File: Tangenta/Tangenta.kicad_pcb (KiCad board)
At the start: 4 copper layers, 243.8 x 243.8 mm, 183 parts, among them J1 39281243, J10 1-2199230-5, J11 TYPEC-304-ACP16, J12 907-211A1019D10200, J13 906-151A1058D10200, J14 RC01133, J16 TF-115K, J17 2309410-1, J18 1-2199230-5, J19 HYC90-SIM06-180, J2 Conn_02x02_Top_Bottom, J3 10018784-10213TLF, J4 10018784-10213TLF, J5 HY911130A, J6 HY911130A, J7 HY911130A, J8 HDMI_19PIN_043, J9 HC-SFP-01L, Q1 2N7002, Q2 2N7002, U1 TPS54331DR, U10 TUSB321RWBR, U11 AOZ1353DI-01, U12 PUSB2X4Y-N, U13 LT8912B, U2 TPS54331DR, U3 TPS54331DR, U4 TPS54331DR, U5 74HC74D,653, U6 CD4060SA_TR, U7 74HC04D,653, U8 USB2514B-I_M2, U9 PUSB2X4Y-N, X1 X322524MOB4SI

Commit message: Lontium - current progress...
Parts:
- added C80: 2.2nF, Capacitor_SMD:C_0402_1005Metric, F.Cu at (358.2, 66.4)
- added OSC1: OT322525MJBA4SL, 25MHZ_OSCILLATOR:25MHZ_OSCILLATOR, F.Cu at (349.7, 78.4)
- added R40: 100k, Resistor_SMD:R_0402_1005Metric, F.Cu at (360.7, 62.4)
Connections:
- U13 pad 1: unconnected-(U13A-MIPIRX0_DP-Pad1) -> /DSI_HDMI/DSI.D0_P
- U13 pad 10: unconnected-(U13A-MIPIRX2_DN-Pad10) -> /DSI_HDMI/DSI.D2_N
- U13 pad 11: unconnected-(U13A-MIPIRX3_DP-Pad11) -> /DSI_HDMI/DSI.D3_P
- U13 pad 12: unconnected-(U13A-MIPIRX3_DN-Pad12) -> /DSI_HDMI/DSI.D3_N
- U13 pad 14: (no net) -> /DSI_HDMI/DSI.HPD
- U13 pad 18: unconnected-(U13B-VDD-Pad18) -> /DSI_HDMI/VDD
- U13 pad 2: unconnected-(U13A-MIPIRX0_DN-Pad2) -> /DSI_HDMI/DSI.D0_N
- U13 pad 26: unconnected-(U13B-VCCA_HDMITX-Pad26) -> /DSI_HDMI/VCCA_HDMITX
- U13 pad 3: unconnected-(U13A-MIPIRX1_DP-Pad3) -> /DSI_HDMI/DSI.D1_P
- U13 pad 33: unconnected-(U13B-VDD-Pad33) -> /DSI_HDMI/VDD
- U13 pad 34: unconnected-(U13B-VCCA_HDMIPLL-Pad34) -> /DSI_HDMI/VCCA_HDMIPLL
- U13 pad 35: unconnected-(U13C-LPF-Pad35) -> Net-(U13C-LPF)
- U13 pad 4: unconnected-(U13A-MIPIRX1_DN-Pad4) -> /DSI_HDMI/DSI.D1_N
- U13 pad 41: unconnected-(U13B-VCCA_LVDSTX-Pad41) -> /DSI_HDMI/VCCA_LVDSTX
- U13 pad 5: unconnected-(U13B-VCCA_MIPIRX-Pad5) -> /DSI_HDMI/VCCA_MIPIRX
- U13 pad 50: unconnected-(U13B-VCCA_SYSCLK-Pad50) -> /DSI_HDMI/VCCA_SYSCLK
- U13 pad 52: unconnected-(U13B-VCCA_LVDSPLL-Pad52) -> /DSI_HDMI/VCCA_LVDSPLL
- U13 pad 57: unconnected-(U13B-VDD-Pad57) -> /DSI_HDMI/VDD
- U13 pad 63: unconnected-(U13C-INT-Pad63) -> /DSI_HDMI/DSI.INT
- U13 pad 64: unconnected-(U13C-RESET_N-Pad64) -> /DSI_HDMI/DSI.nRST
- U13 pad 7: unconnected-(U13A-MIPIRX_CKP-Pad7) -> /DSI_HDMI/DSI.CLK_P
- U13 pad 8: unconnected-(U13A-MIPIRX_CKN-Pad8) -> /DSI_HDMI/DSI.CLK_N
- U13 pad 9: unconnected-(U13A-MIPIRX2_DP-Pad9) -> /DSI_HDMI/DSI.D2_P

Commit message: DSI_HDMI current progress...
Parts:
- added C81: 10uF, Capacitor_SMD:C_0402_1005Metric, F.Cu at (338.1, 92.8)
- added C82: 100nF, Capacitor_SMD:C_0402_1005Metric, F.Cu at (338.1, 94.8)
- added C83: 10nF, Capacitor_SMD:C_0402_1005Metric, F.Cu at (338.1, 96.8)
- added FB9: GZ2012D101TF, Ferrite_Bead_100:Ferrite_Bead_100, F.Cu at (342.1, 93.5)
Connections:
- J17 pad 17: unconnected-(J17-Pad17) -> /DSI_HDMI/DSI.INT
- J17 pad 19: unconnected-(J17-Pad19) -> /DSI_HDMI/DSI.HPD
- J17 pad 21: unconnected-(J17-Pad21) -> /DSI_HDMI/DSI.nRST
- J17 pad 23: unconnected-(J17-Pad23) -> /DSI_HDMI/DSI.D3_N
- J17 pad 25: unconnected-(J17-Pad25) -> /DSI_HDMI/DSI.D3_P
- J17 pad 29: unconnected-(J17-Pad29) -> /DSI_HDMI/DSI.D2_N
- J17 pad 31: unconnected-(J17-Pad31) -> /DSI_HDMI/DSI.D2_P
- J17 pad 35: unconnected-(J17-Pad35) -> /DSI_HDMI/DSI.CLK_N
- J17 pad 37: unconnected-(J17-Pad37) -> /DSI_HDMI/DSI.CLK_P
- J17 pad 41: unconnected-(J17-Pad41) -> /DSI_HDMI/DSI.D1_N
- J17 pad 42: unconnected-(J17-Pad42) -> /DSI_HDMI/I2S.BCLK
- J17 pad 43: unconnected-(J17-Pad43) -> /DSI_HDMI/DSI.D1_P
- J17 pad 44: unconnected-(J17-Pad44) -> /DSI_HDMI/I2S.SYNC
- J17 pad 46: unconnected-(J17-Pad46) -> /DSI_HDMI/I2S.D_OUT
- J17 pad 47: unconnected-(J17-Pad47) -> /DSI_HDMI/DSI.D0_N
- J17 pad 49: unconnected-(J17-Pad49) -> /DSI_HDMI/DSI.D0_P
- OSC1 pad 1: unconnected-(OSC1-Enable/Disable-Pad1) -> Net-(OSC1-Enable/Disable)
- OSC1 pad 2: unconnected-(OSC1-GND-Pad2) -> GNDREF
- OSC1 pad 3: unconnected-(OSC1-OUT-Pad3) -> /DSI_HDMI/XTALI
- OSC1 pad 4: unconnected-(OSC1-VDD-Pad4) -> Net-(OSC1-Enable/Disable)
- U13 pad 53: unconnected-(U13A-XTALI-Pad53) -> /DSI_HDMI/XTALI
- U13 pad 58: unconnected-(U13C-SD0_CEC-Pad58) -> /DSI_HDMI/I2S.D_OUT
- U13 pad 59: unconnected-(U13C-WS_I-Pad59) -> /DSI_HDMI/I2S.SYNC
- U13 pad 60: unconnected-(U13C-SCLK_I-Pad60) -> /DSI_HDMI/I2S.BCLK

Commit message: Current progress...
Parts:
- added R41: 1.8k, Resistor_SMD:R_0402_1005Metric, F.Cu at (373.0, 63.9)
- added R42: 1.8k, Resistor_SMD:R_0402_1005Metric, F.Cu at (373.0, 65.9)
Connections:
- J17 pad 12: unconnected-(J17-Pad12) -> /Toradex/I2C.SDA
- J17 pad 14: unconnected-(J17-Pad14) -> /Toradex/I2C.SCL
- U13 pad 61: unconnected-(U13C-S_SDA-Pad61) -> /DSI_HDMI/I2C.SDA
- U13 pad 62: unconnected-(U13C-S_SCL-Pad62) -> /DSI_HDMI/I2C.SCL
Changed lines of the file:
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@@
   (net 648 "unconnected-(J17-Pad10)")
   (net 649 "unconnected-(J17-Pad11)")
-  (net 650 "unconnected-(J17-Pad12)")
+  (net 650 "/Toradex/I2C.SDA")
   (net 651 "unconnected-(J17-Pad13)")
-  (net 652 "unconnected-(J17-Pad14)")
+  (net 652 "/Toradex/I2C.SCL")
   (net 653 "unconnected-(J17-Pad15)")
   (net 654 "unconnected-(J17-Pad16)")
@@
   (net 1033 "unconnected-(U13C-XTALO-Pad54)")
   (net 1034 "unconnected-(U13C-REFCLK-Pad55)")
-  (net 1035 "unconnected-(U13C-S_SDA-Pad61)")
-  (net 1036 "unconnected-(U13C-S_SCL-Pad62)")
+  (net 1035 "/DSI_HDMI/I2C.SDA")
+  (net 1036 "/DSI_HDMI/I2C.SCL")
   (net 1037 "/DSI_HDMI/DSI.D3_N")
   (net 1038 "/DSI_HDMI/DSI.HPD")
@@
       (net 649 "unconnected-(J17-Pad11)") (pinfunction "11") (pintype "passive"))
     (pad "12" smd rect (at -30.625 -12.025 180) (size 0.3 1.75) (layers "F.Cu" "F.Paste" "F.Mask")
-      (net 650 "unconnected-(J17-Pad12)") (pinfunction "12") (pintype "passive"))
+      (net 650 "/Toradex/I2C.SDA") (pinfunction "12") (pintype "passive"))
     (pad "13" smd rect (at -30.375 -3.825 180) (size 0.3 1.75) (layers "F.Cu" "F.Paste" "F.Mask")
       (net 651 "unconnected-(J17-Pad13)") (pinfunction "13") (pintype "passive"))
     (pad "14" smd rect (at -30.125 -12.025 180) (size 0.3 1.75) (layers "F.Cu" "F.Paste" "F.Mask")
-      (net 652 "unconnected-(J17-Pad14)") (pinfunction "14") (pintype "passive"))
+      (net 652 "/Toradex/I2C.SCL") (pinfunction "14") (pintype "passive"))
     (pad "15" smd rect (at -29.875 -3.825 180) (size 0.3 1.75) (layers "F.Cu" "F.Paste" "F.Mask")
       (net 653 "unconnected-(J17-Pad15)") (pinfunction "15") (pintype "passive"))
@@
       (net 655 "/DSI_HDMI/I2S.BCLK") (pinfunction "SCLK_I") (pintype "unspecified") (thermal_bridge_angle 45))
     (pad "61" smd oval (at -1.8 -3.7) (size 0.2 0.7) (layers "F.Cu" "F.Paste" "F.Mask")
-      (net 1035 "unconnected-(U13C-S_SDA-Pad61)") (pinfunction "S_SDA") (pintype "unspecified") (thermal_bridge_angle 45))
+      (net 1035 "/DSI_HDMI/I2C.SDA") (pinfunction "S_SDA") (pintype "unspecified") (thermal_bridge_angle 45))
     (pad "62" smd oval (at -2.2 -3.7) (size 0.2 0.7) (layers "F.Cu" "F.Paste" "F.Mask")
-      (net 1036 "unconnected-(U13C-S_SCL-Pad62)") (pinfunction "S_SCL") (pintype "unspecified") (thermal_bridge_angle 45))
+      (net 1036 "/DSI_HDMI/I2C.SCL") (pinfunction "S_SCL") (pintype "unspecified") (thermal_bridge_angle 45))
     (pad "63" smd oval (at -2.6 -3.7) (size 0.2 0.7) (layers "F.Cu" "F.Paste" "F.Mask")
       (net 988 "/DSI_HDMI/DSI.INT") (pinfunction "INT") (pintype "unspecified") (thermal_bridge_angle 45))
@@
     )
   )
+  (footprint "Resistor_SMD:R_0402_1005Metric" (layer "F.Cu")
+    (at 372.997 63.923)
+    (descr "Resistor SMD 0402 (1005 Metric), square (rectangular) end terminal, IPC_7351 nominal, (Body size source: IPC-SM-782 page 72, https://www.pcb-3d.com/wordpress/wp-content/uploads/ipc-sm-782a_amendment_1_and_2.pdf), generated with kicad-footprint-generator")
+    (tags "resistor")
+    (property "Sheetfile" "DSI_HDMI.kicad_sch")
+    (property "Sheetname" "DSI_HDMI")
+    (property "ki_description" "Resistor, small US symbol")
+    (property "ki_keywords" "r resistor")
+    (attr smd)
+    (fp_text reference "R41" (at 0 -1.17) (layer "F.SilkS")
+        (effects (font (size 1 1) (thickness 0.15)))
+    )
+    (fp_text value "1.8k" (at 0 1.17) (layer "F.Fab")
+        (effects (font (size 1 1) (thickness 0.15)))
+    )
+    (fp_text user "${REFERENCE}" (at 0 0) (layer "F.Fab")
+        (effects (font (size 0.26 0.26) (thickness 0.04)))
+    )
+    (fp_line (start -0.153641 -0.38) (end 0.153641 -0.38)
+      (stroke (width 0.12) (type solid)) (layer "F.SilkS"))
+    (fp_line (start -0.153641 0.38) (end 0.153641 0.38)
+      (stroke (width 0.12) (type solid)) (layer "F.SilkS"))
+    (fp_line (start -0.93 -0.47) (end 0.93 -0.47)
+      (stroke (width 0.05) (type solid)) (layer "F.CrtYd"))
+    (fp_line (start -0.93 0.47) (end -0.93 -0.47)
+      (stroke (width 0.05) (type solid)) (layer "F.CrtYd"))
+    (fp_line (start 0.93 -0.47) (end 0.93 0.47)
+      (stroke (width 0.05) (type solid)) (layer "F.CrtYd"))
+    (fp_line (start 0.93 0.47) (end -0.93 0.47)
+      (stroke (width 0.05) (type solid)) (layer "F.CrtYd"))
+    (fp_line (start -0.525 -0.27) (end 0.525 -0.27)
+      (stroke (width 0.1) (type solid)) (layer "F.Fab"))
+    (fp_line (start -0.525 0.27) (end -0.525 -0.27)
+      (stroke (width 0.1) (type solid)) (layer "F.Fab"))
+    (fp_line (start 0.525 -0.27) (end 0.525 0.27)
+      (stroke (width 0.1) (type solid)) (layer "F.Fab"))
+    (fp_line (start 0.525 0.27) (end -0.525 0.27)
+      (stroke (width 0.1) (type solid)) (layer "F.Fab"))
+    (pad "1" smd roundrect (at -0.51 0) (size 0.54 0.64) (layers "F.Cu" "F.Paste" "F.Mask") (roundrect_rratio 0.25)
+      (net 1035 "/DSI_HDMI/I2C.SDA") (pintype "passive"))
+    (pad "2" smd roundrect (at 0.51 0) (size 0.54 0.64) (layers "F.Cu" "F.Paste" "F.Mask") (roundrect_rratio 0.25)
+      (net 987 "/DSI_HDMI/1V8") (pintype "passive"))
+    (model "${KICAD6_3DMODEL_DIR}/Resistor_SMD.3dshapes/R_0402_1005Metric.wrl"
+      (offset (xyz 0 0 0))
+      (scale (xyz 1 1 1))
+      (rotate (xyz 0 0 0))
+    )
+  )
   (footprint "CAP_TANTAL_A:CAP_TANTAL_A" (layer "F.Cu")
     (at 264.1722 65.9638)
@@
       (offset (xyz 0 0 0))
       (scale (xyz 1 1 1))
+      (rotate (xyz 0 0 0))
+    )
+  )
+  (footprint "Resistor_SMD:R_0402_1005Metric" (layer "F.Cu")
+    (at 372.997 65.913)
+    (descr "Resistor SMD 0402 (1005 Metric), square (rectangular) end terminal, IPC_7351 nominal, (Body size source: IPC-SM-782 page 72, https://www.pcb-3d.com/wordpress/wp-content/uploads/ipc-sm-782a_amendment_1_and_2.pdf), generated with kicad-footprint-generator")
+    (tags "resistor")
+    (property "Sheetfile" "DSI_HDMI.kicad_sch")
+    (property "Sheetname" "DSI_HDMI")
+    (property "ki_description" "Resistor, small US symbol")
+    (property "ki_keywords" "r resistor")
+    (attr smd)
+    (fp_text reference "R42" (at 0 -1.17) (layer "F.SilkS")
+        (effects (font (size 1 1) (thickness 0.15)))
+    )
+    (fp_text value "1.8k" (at 0 1.17) (layer "F.Fab")
+        (effects (font (size 1 1) (thickness 0.15)))
+    )
+    (fp_text user "${REFERENCE}" (at 0 0) (layer "F.Fab")
+        (effects (font (size 0.26 0.26) (thickness 0.04)))
+    )
+    (fp_line (start -0.153641 -0.38) (end 0.153641 -0.38)
+      (stroke (width 0.12) (type solid)) (layer "F.SilkS"))
+    (fp_line (start -0.153641 0.38) (end 0.153641 0.38)
+      (stroke (width 0.12) (type solid)) (layer "F.SilkS"))
+    (fp_line (start -0.93 -0.47) (end 0.93 -0.47)
+      (stroke (width 0.05) (type solid)) (layer "F.CrtYd"))
+    (fp_line (start -0.93 0.47) (end -0.93 -0.47)
+      (stroke (width 0.05) (type solid)) (layer "F.CrtYd"))
+    (fp_line (start 0.93 -0.47) (end 0.93 0.47)
+      (stroke (width 0.05) (type solid)) (layer "F.CrtYd"))
+    (fp_line (start 0.93 0.47) (end -0.93 0.47)
+      (stroke (width 0.05) (type solid)) (layer "F.CrtYd"))
+    (fp_line (start -0.525 -0.27) (end 0.525 -0.27)
+      (stroke (width 0.1) (type solid)) (layer "F.Fab"))
+    (fp_line (start -0.525 0.27) (end -0.525 -0.27)
+      (stroke (width 0.1) (type solid)) (layer "F.Fab"))
+    (fp_line (start 0.525 -0.27) (end 0.525 0.27)
+      (stroke (width 0.1) (type solid)) (layer "F.Fab"))
+    (fp_line (start 0.525 0.27) (end -0.525 0.27)
+      (stroke (width 0.1) (type solid)) (layer "F.Fab"))
+    (pad "1" smd roundrect (at -0.51 0) (size 0.54 0.64) (layers "F.Cu" "F.Paste" "F.Mask") (roundrect_rratio 0.25)
+      (net 1036 "/DSI_HDMI/I2C.SCL") (pintype "passive"))
+    (pad "2" smd roundrect (at 0.51 0) (size 0.54 0.64) (layers "F.Cu" "F.Paste" "F.Mask") (roundrect_rratio 0.25)
+      (net 987 "/DSI_HDMI/1V8") (pintype "passive"))
+    (model "${KICAD6_3DMODEL_DIR}/Resistor_SMD.3dshapes/R_0402_1005Metric.wrl"
+      (offset (xyz 0 0 0))
+      (scale (xyz 1 1 1))

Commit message: ...
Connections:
- J17 pad 12: /Toradex/I2C.SDA -> /DSI_HDMI/I2C.SDA
- J17 pad 14: /Toradex/I2C.SCL -> /DSI_HDMI/I2C.SCL

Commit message: ...
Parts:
- added R43: 6k, Resistor_SMD:R_0402_1005Metric, F.Cu at (367.4, 73.0)
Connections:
- U13 pad 13: unconnected-(U13C-R6K-Pad13) -> Net-(U13C-R6K)
- U13 pad 17: unconnected-(U13B-VSS-Pad17) -> GNDREF
- U13 pad 23: unconnected-(U13B-VSSA_HDMITX-Pad23) -> GNDREF
- U13 pad 29: unconnected-(U13B-VSSA_HDMITX-Pad29) -> GNDREF
- U13 pad 32: unconnected-(U13B-VSS-Pad32) -> GNDREF
- U13 pad 36: unconnected-(U13B-VSSA_HDMIPLL-Pad36) -> GNDREF
- U13 pad 42: unconnected-(U13B-VSSA_LVDSTX-Pad42) -> GNDREF
- U13 pad 49: unconnected-(U13B-VSSA_SYSCLK-Pad49) -> GNDREF
- U13 pad 51: unconnected-(U13B-VSSA_LVDSPLL-Pad51) -> GNDREF
- U13 pad 55: unconnected-(U13C-REFCLK-Pad55) -> GNDREF
- U13 pad 56: (no net) -> GNDREF
- U13 pad 6: unconnected-(U13B-VSSA_MIPIRX-Pad6) -> GNDREF
- U13 pad 65: unconnected-(U13B-EPAD-Pad65) -> GNDREF

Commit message: ...
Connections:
- net /DSI_HDMI/I2C.SCL renamed /DSI_HDMI/I2C_1.SCL
- net /DSI_HDMI/I2C.SDA renamed /DSI_HDMI/I2C_1.SDA
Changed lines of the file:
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@@
   (net 1021 "unconnected-(U13A-LVDSTX0_DN-Pad48)")
   (net 1022 "unconnected-(U13C-XTALO-Pad54)")
-  (net 1023 "/DSI_HDMI/I2C.SDA")
-  (net 1024 "/DSI_HDMI/I2C.SCL")
-  (net 1025 "/DSI_HDMI/DSI.D3_N")
-  (net 1026 "/DSI_HDMI/DSI.HPD")
-  (net 1027 "/DSI_HDMI/DSI.nRST")
+  (net 1023 "/DSI_HDMI/DSI.D3_N")
+  (net 1024 "/DSI_HDMI/DSI.HPD")
+  (net 1025 "/DSI_HDMI/DSI.nRST")
+  (net 1026 "/DSI_HDMI/I2C_1.SDA")
+  (net 1027 "/DSI_HDMI/I2C_1.SCL")
   (footprint "Resistor_SMD:R_0402_1005Metric" (layer "F.Cu")
     (at 76.837 35.687)
@@
       (net 649 "unconnected-(J17-Pad11)") (pinfunction "11") (pintype "passive"))
     (pad "12" smd rect (at -30.625 -12.025 180) (size 0.3 1.75) (layers "F.Cu" "F.Paste" "F.Mask")
-      (net 1023 "/DSI_HDMI/I2C.SDA") (pinfunction "12") (pintype "passive"))
+      (net 1026 "/DSI_HDMI/I2C_1.SDA") (pinfunction "12") (pintype "passive"))
     (pad "13" smd rect (at -30.375 -3.825 180) (size 0.3 1.75) (layers "F.Cu" "F.Paste" "F.Mask")
       (net 650 "unconnected-(J17-Pad13)") (pinfunction "13") (pintype "passive"))
     (pad "14" smd rect (at -30.125 -12.025 180) (size 0.3 1.75) (layers "F.Cu" "F.Paste" "F.Mask")
-      (net 1024 "/DSI_HDMI/I2C.SCL") (pinfunction "14") (pintype "passive"))
+      (net 1027 "/DSI_HDMI/I2C_1.SCL") (pinfunction "14") (pintype "passive"))
     (pad "15" smd rect (at -29.875 -3.825 180) (size 0.3 1.75) (layers "F.Cu" "F.Paste" "F.Mask")
       (net 651 "unconnected-(J17-Pad15)") (pinfunction "15") (pintype "passive"))
@@
       (net 654 "unconnected-(J17-Pad18)") (pinfunction "18") (pintype "passive"))
     (pad "19" smd rect (at -28.875 -3.825 180) (size 0.3 1.75) (layers "F.Cu" "F.Paste" "F.Mask")
-      (net 1026 "/DSI_HDMI/DSI.HPD") (pinfunction "19") (pintype "passive"))
+      (net 1024 "/DSI_HDMI/DSI.HPD") (pinfunction "19") (pintype "passive"))
     (pad "20" smd rect (at -28.625 -12.025 180) (size 0.3 1.75) (layers "F.Cu" "F.Paste" "F.Mask")
       (net 656 "unconnected-(J17-Pad20)") (pinfunction "20") (pintype "passive"))
     (pad "21" smd rect (at -28.375 -3.825 180) (size 0.3 1.75) (layers "F.Cu" "F.Paste" "F.Mask")
-      (net 1027 "/DSI_HDMI/DSI.nRST") (pinfunction "21") (pintype "passive"))
+      (net 1025 "/DSI_HDMI/DSI.nRST") (pinfunction "21") (pintype "passive"))
     (pad "22" smd rect (at -28.125 -12.025 180) (size 0.3 1.75) (layers "F.Cu" "F.Paste" "F.Mask")
       (net 658 "unconnected-(J17-Pad22)") (pinfunction "22") (pintype "passive"))
     (pad "23" smd rect (at -27.875 -3.825 180) (size 0.3 1.75) (layers "F.Cu" "F.Paste" "F.Mask")
-      (net 1025 "/DSI_HDMI/DSI.D3_N") (pinfunction "23") (pintype "passive"))
+      (net 1023 "/DSI_HDMI/DSI.D3_N") (pinfunction "23") (pintype "passive"))
     (pad "24" smd rect (at -27.625 -12.025 180) (size 0.3 1.75) (layers "F.Cu" "F.Paste" "F.Mask")
       (net 659 "unconnected-(J17-Pad24)") (pinfunction "24") (pintype "passive"))
@@
       (net 997 "/DSI_HDMI/DSI.D3_P") (pinfunction "MIPIRX3_DP") (pintype "unspecified") (thermal_bridge_angle 45))
     (pad "12" smd oval (at -3.7 1.4 90) (size 0.2 0.7) (layers "F.Cu" "F.Paste" "F.Mask")
-      (net 1025 "/DSI_HDMI/DSI.D3_N") (pinfunction "MIPIRX3_DN") (pintype "unspecified") (thermal_bridge_angle 45))
+      (net 1023 "/DSI_HDMI/DSI.D3_N") (pinfunction "MIPIRX3_DN") (pintype "unspecified") (thermal_bridge_angle 45))
     (pad "13" smd oval (at -3.7 1.8 90) (size 0.2 0.7) (layers "F.Cu" "F.Paste" "F.Mask")
       (net 991 "Net-(U13C-R6K)") (pinfunction "R6K") (pintype "unspecified") (thermal_bridge_angle 45))
     (pad "14" smd oval (at -3.7 2.2 90) (size 0.2 0.7) (layers "F.Cu" "F.Paste" "F.Mask")
-      (net 1026 "/DSI_HDMI/DSI.HPD") (pinfunction "HPD") (pintype "unspecified") (thermal_bridge_angle 45))
+      (net 1024 "/DSI_HDMI/DSI.HPD") (pinfunction "HPD") (pintype "unspecified") (thermal_bridge_angle 45))
     (pad "15" smd oval (at -3.7 2.6 90) (size 0.2 0.7) (layers "F.Cu" "F.Paste" "F.Mask")
       (net 998 "unconnected-(U13C-VBUS-Pad15)") (pinfunction "VBUS") (pintype "unspecified+no_connect") (thermal_bridge_angle 45))
@@
       (net 653 "/DSI_HDMI/I2S.BCLK") (pinfunction "SCLK_I") (pintype "unspecified") (thermal_bridge_angle 45))
     (pad "61" smd oval (at -1.8 -3.7) (size 0.2 0.7) (layers "F.Cu" "F.Paste" "F.Mask")
-      (net 1023 "/DSI_HDMI/I2C.SDA") (pinfunction "S_SDA") (pintype "unspecified") (thermal_bridge_angle 45))
+      (net 1026 "/DSI_HDMI/I2C_1.SDA") (pinfunction "S_SDA") (pintype "unspecified") (thermal_bridge_angle 45))
     (pad "62" smd oval (at -2.2 -3.7) (size 0.2 0.7) (layers "F.Cu" "F.Paste" "F.Mask")
-      (net 1024 "/DSI_HDMI/I2C.SCL") (pinfunction "S_SCL") (pintype "unspecified") (thermal_bridge_angle 45))
+      (net 1027 "/DSI_HDMI/I2C_1.SCL") (pinfunction "S_SCL") (pintype "unspecified") (thermal_bridge_angle 45))
     (pad "63" smd oval (at -2.6 -3.7) (size 0.2 0.7) (layers "F.Cu" "F.Paste" "F.Mask")
       (net 986 "/DSI_HDMI/DSI.INT") (pinfunction "INT") (pintype "unspecified") (thermal_bridge_angle 45))
     (pad "64" smd oval (at -3 -3.7) (size 0.2 0.7) (layers "F.Cu" "F.Paste" "F.Mask")
-      (net 1027 "/DSI_HDMI/DSI.nRST") (pinfunction "RESET_N") (pintype "unspecified") (thermal_bridge_angle 45))
+      (net 1025 "/DSI_HDMI/DSI.nRST") (pinfunction "RESET_N") (pintype "unspecified") (thermal_bridge_angle 45))
     (pad "65" thru_hole circle (at -1.9 -1.9) (size 1 1) (drill 0.5) (layers "*.Cu" "*.Mask")
       (net 5 "GNDREF") (pinfunction "EPAD") (pintype "unspecified"))
@@
       (stroke (width 0.1) (type solid)) (layer "F.Fab"))
     (pad "1" smd roundrect (at -0.51 0) (size 0.54 0.64) (layers "F.Cu" "F.Paste" "F.Mask") (roundrect_rratio 0.25)
-      (net 1023 "/DSI_HDMI/I2C.SDA") (pintype "passive"))
+      (net 1026 "/DSI_HDMI/I2C_1.SDA") (pintype "passive"))
     (pad "2" smd roundrect (at 0.51 0) (size 0.54 0.64) (layers "F.Cu" "F.Paste" "F.Mask") (roundrect_rratio 0.25)
       (net 985 "/DSI_HDMI/1V8") (pintype "passive"))
@@
       (stroke (width 0.1) (type solid)) (layer "F.Fab"))
     (pad "1" smd roundrect (at -0.51 0) (size 0.54 0.64) (layers "F.Cu" "F.Paste" "F.Mask") (roundrect_rratio 0.25)
-      (net 1024 "/DSI_HDMI/I2C.SCL") (pintype "passive"))
+      (net 1027 "/DSI_HDMI/I2C_1.SCL") (pintype "passive"))
     (pad "2" smd roundrect (at 0.51 0) (size 0.54 0.64) (layers "F.Cu" "F.Paste" "F.Mask") (roundrect_rratio 0.25)
       (net 985 "/DSI_HDMI/1V8") (pintype "passive"))

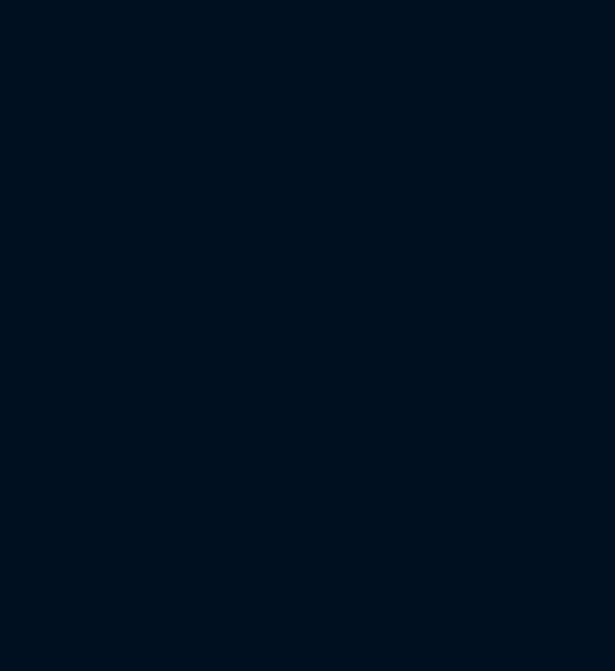
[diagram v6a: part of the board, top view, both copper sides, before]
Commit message: HDMI port I2C with level shifter.
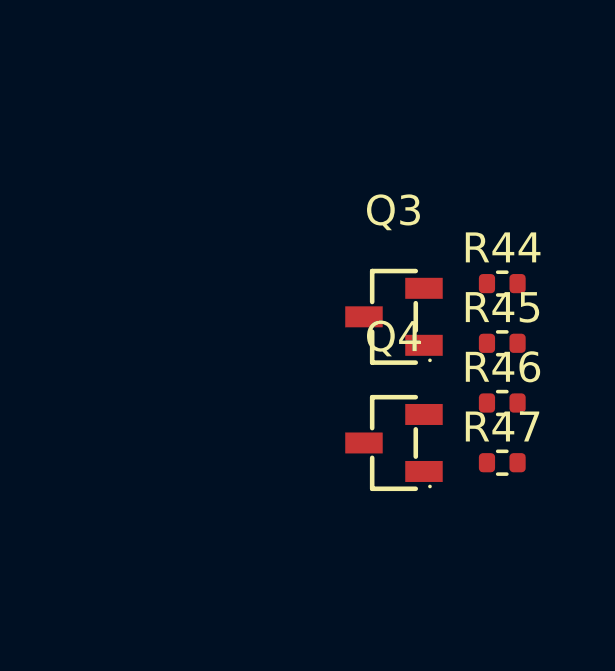
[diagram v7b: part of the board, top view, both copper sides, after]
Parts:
- added Q3: 2N7002, NMOS_2N7002:NMOS_2N7002, F.Cu at (369.5, 97.2)
- added Q4: 2N7002, NMOS_2N7002:NMOS_2N7002, F.Cu at (369.5, 101.5)
- added R44: 1.8k, Resistor_SMD:R_0402_1005Metric, F.Cu at (373.1, 96.1)
- added R45: 1.8k, Resistor_SMD:R_0402_1005Metric, F.Cu at (373.1, 98.1)
- added R46: 2k, Resistor_SMD:R_0402_1005Metric, F.Cu at (373.1, 100.1)
- added R47: 4.7k, Resistor_SMD:R_0402_1005Metric, F.Cu at (373.1, 102.1)
